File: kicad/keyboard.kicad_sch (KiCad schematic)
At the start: 1 part, among them J1 Conn_02x06_Odd_Even

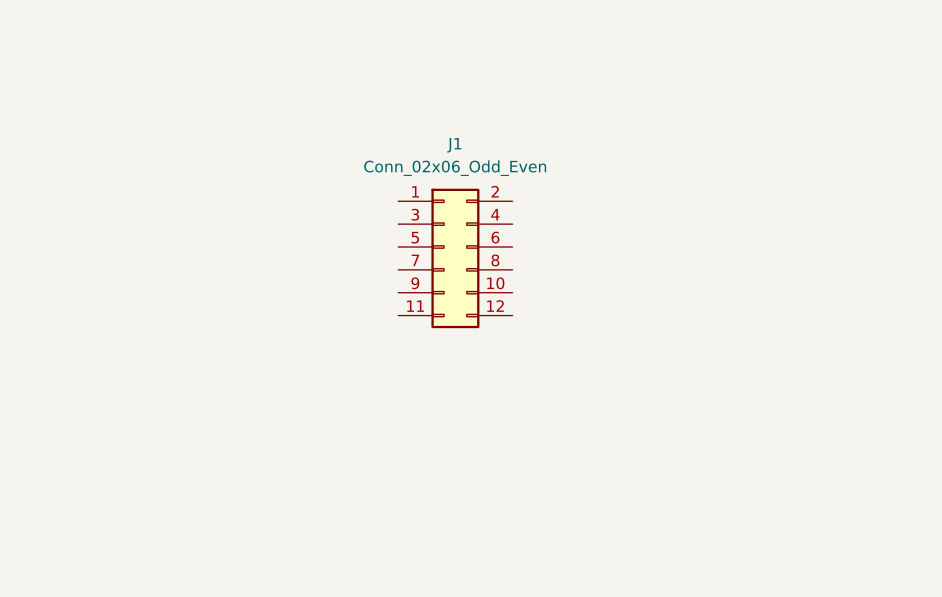
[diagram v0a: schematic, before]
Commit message: Add keyboard connector
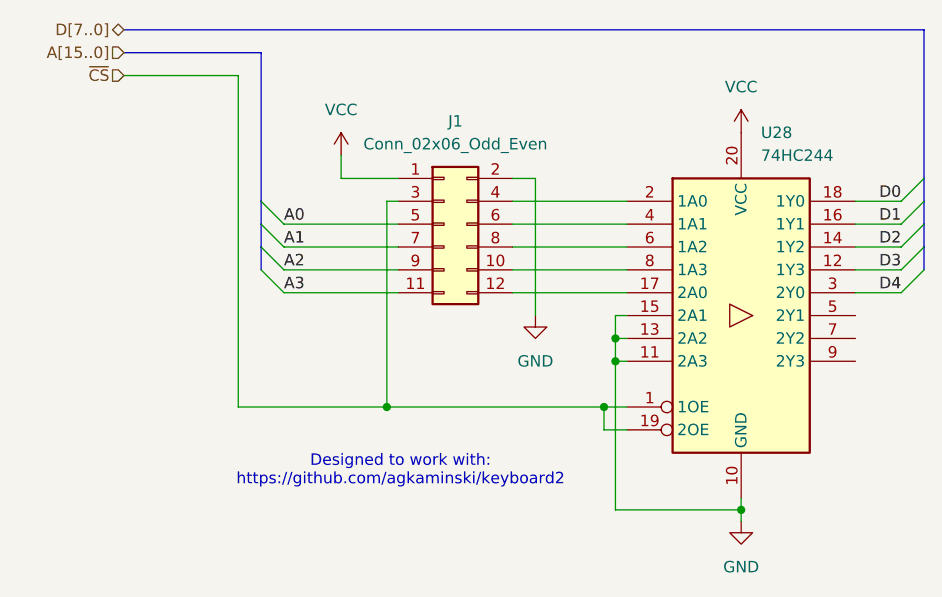
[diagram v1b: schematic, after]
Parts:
- added U28: 74HC244, symbol 74xx:74HC244
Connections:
- net VCC: now reaches J1.1 (Pin_1)
- net VCC: now also U28.20 (VCC)
- net at J1.10 (Pin_10): now also U28.8 (1A3)
- net A3: now reaches J1.11 (Pin_11)
- net at J1.12 (Pin_12): now also U28.17 (2A0)
- net GND: now reaches J1.2 (Pin_2)
- net GND: now also U28.10 (GND), U28.11 (2A3), U28.13 (2A2), U28.15 (2A1)
- net ~{CS}: now reaches J1.3 (Pin_3)
- net ~{CS}: now also U28.1 (1OE), U28.19 (2OE)
- net at J1.4 (Pin_4): now also U28.2 (1A0)
- net A0: now reaches J1.5 (Pin_5)
- net at J1.6 (Pin_6): now also U28.4 (1A1)
- net A1: now reaches J1.7 (Pin_7)
- net at J1.8 (Pin_8): now also U28.6 (1A2)
- net A2: now reaches J1.9 (Pin_9)
- new net D0: U28.18 (1Y0)
- new net D1: U28.16 (1Y1)
- new net D2: U28.14 (1Y2)
- new net D3: U28.12 (1Y3)
- new net D4: U28.3 (2Y0)
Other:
- note added: "Designed to work with: https://github.com/agkaminski/keyboard2"
- moved on the sheet: J1

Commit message: Add user IO and USB
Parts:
- U28: footprint (none) -> Package_DIP:DIP-20_W7.62mm
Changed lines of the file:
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@@
 			)
 		)
-		(property "Footprint" ""
+		(property "Footprint" "Package_DIP:DIP-20_W7.62mm"
 			(at 165.1 129.54 0)
 			(effects

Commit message: Add caps and make initial placement
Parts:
- added C37: 100n, Capacitor_THT:C_Disc_D5.0mm_W2.5mm_P2.50mm, symbol Device:C
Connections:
- net GND: now also C37.2
- net VCC: now also C37.1
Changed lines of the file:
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@@
+	(symbol
+		(lib_id "power:VCC")
+		(at 182.88 143.51 0)
+		(unit 1)
+		(exclude_from_sim no)
+		(in_bom yes)
+		(on_board yes)
+		(dnp no)
+		(fields_autoplaced yes)
+		(property "Reference" "#PWR0157"
+			(at 182.88 147.32 0)
+			(effects
+				(font
+					(size 1.27 1.27)
+				)
+				(hide yes)
+			)
+		)
+		(property "Value" "VCC"
+			(at 182.88 138.43 0)
+			(effects
+				(font
+					(size 1.27 1.27)
+				)
+			)
+		)
+		(property "Footprint" ""
+			(at 182.88 143.51 0)
+			(effects
+				(font
+					(size 1.27 1.27)
+				)
+				(hide yes)
+			)
+		)
+		(property "Datasheet" ""
+			(at 182.88 143.51 0)
+			(effects
+				(font
+					(size 1.27 1.27)
+				)
+				(hide yes)
+			)
+		)
+		(property "Description" "Power symbol creates a global label with name \"VCC\""
+			(at 182.88 143.51 0)
+			(effects
+				(font
+					(size 1.27 1.27)
+				)
+				(hide yes)
+			)
+		)
+		(pin "1"
+		)
+		(instances
+			(project "fella"
+				(path "/0e49b66d-39aa-4a48-b9a1-8037366b6d94/4fcf83d0-a396-4aeb-b2db-c20a053d3b3c"
+					(reference "#PWR0157")
+					(unit 1)
+				)
+			)
+		)
+	)
+	(symbol
+		(lib_id "power:GND")
+		(at 182.88 151.13 0)
+		(unit 1)
+		(exclude_from_sim no)
+		(in_bom yes)
+		(on_board yes)
+		(dnp no)
+		(fields_autoplaced yes)
+		(property "Reference" "#PWR0158"
+			(at 182.88 157.48 0)
+			(effects
+				(font
+					(size 1.27 1.27)
+				)
+				(hide yes)
+			)
+		)
+		(property "Value" "GND"
+			(at 182.88 156.21 0)
+			(effects
+				(font
+					(size 1.27 1.27)
+				)
+			)
+		)
+		(property "Footprint" ""
+			(at 182.88 151.13 0)
+			(effects
+				(font
+					(size 1.27 1.27)
+				)
+				(hide yes)
+			)
+		)
+		(property "Datasheet" ""
+			(at 182.88 151.13 0)
+			(effects
+				(font
+					(size 1.27 1.27)
+				)
+				(hide yes)
+			)
+		)
+		(property "Description" "Power symbol creates a global label with name \"GND\" , ground"
+			(at 182.88 151.13 0)
+			(effects
+				(font
+					(size 1.27 1.27)
+				)
+				(hide yes)
+			)
+		)
+		(pin "1"
+		)
+		(instances
+			(project "fella"
+				(path "/0e49b66d-39aa-4a48-b9a1-8037366b6d94/4fcf83d0-a396-4aeb-b2db-c20a053d3b3c"
+					(reference "#PWR0158")
+					(unit 1)
+				)
+			)
+		)
+	)
 	(symbol
 		(lib_id "power:VCC")
@@
 					(unit 1)
 				)
+			)
+		)
+	)
+	(symbol
+		(lib_id "Device:C")
+		(at 182.88 147.32 0)
+		(unit 1)
+		(exclude_from_sim no)
+		(in_bom yes)
+		(on_board yes)
+		(dnp no)
+		(fields_autoplaced yes)
+		(property "Reference" "C37"
+			(at 186.69 146.0499 0)
+			(effects
+				(font
+					(size 1.27 1.27)
+				)
+				(justify left)
+			)
+		)
+		(property "Value" "100n"
+			(at 186.69 148.5899 0)
+			(effects
+				(font
+					(size 1.27 1.27)
+				)
+				(justify left)
+			)
+		)
+		(property "Footprint" "Capacitor_THT:C_Disc_D5.0mm_W2.5mm_P2.50mm"
+			(at 183.8452 151.13 0)
+			(effects
+				(font
+					(size 1.27 1.27)
+				)
+				(hide yes)
+			)
+		)
+		(property "Datasheet" "~"
+			(at 182.88 147.32 0)
+			(effects
+				(font
+					(size 1.27 1.27)
+				)
+				(hide yes)
+			)
+		)
+		(property "Description" "Unpolarized capacitor"
+			(at 182.88 147.32 0)
+			(effects
+				(font
+					(size 1.27 1.27)
+				)
+				(hide yes)
+			)
+		)
+		(pin "2"
+		)
+		(pin "1"
+		)
+		(instances
+			(project "fella"
+				(path "/0e49b66d-39aa-4a48-b9a1-8037366b6d94/4fcf83d0-a396-4aeb-b2db-c20a053d3b3c"
+					(reference "C37")
+					(unit 1)
+				)

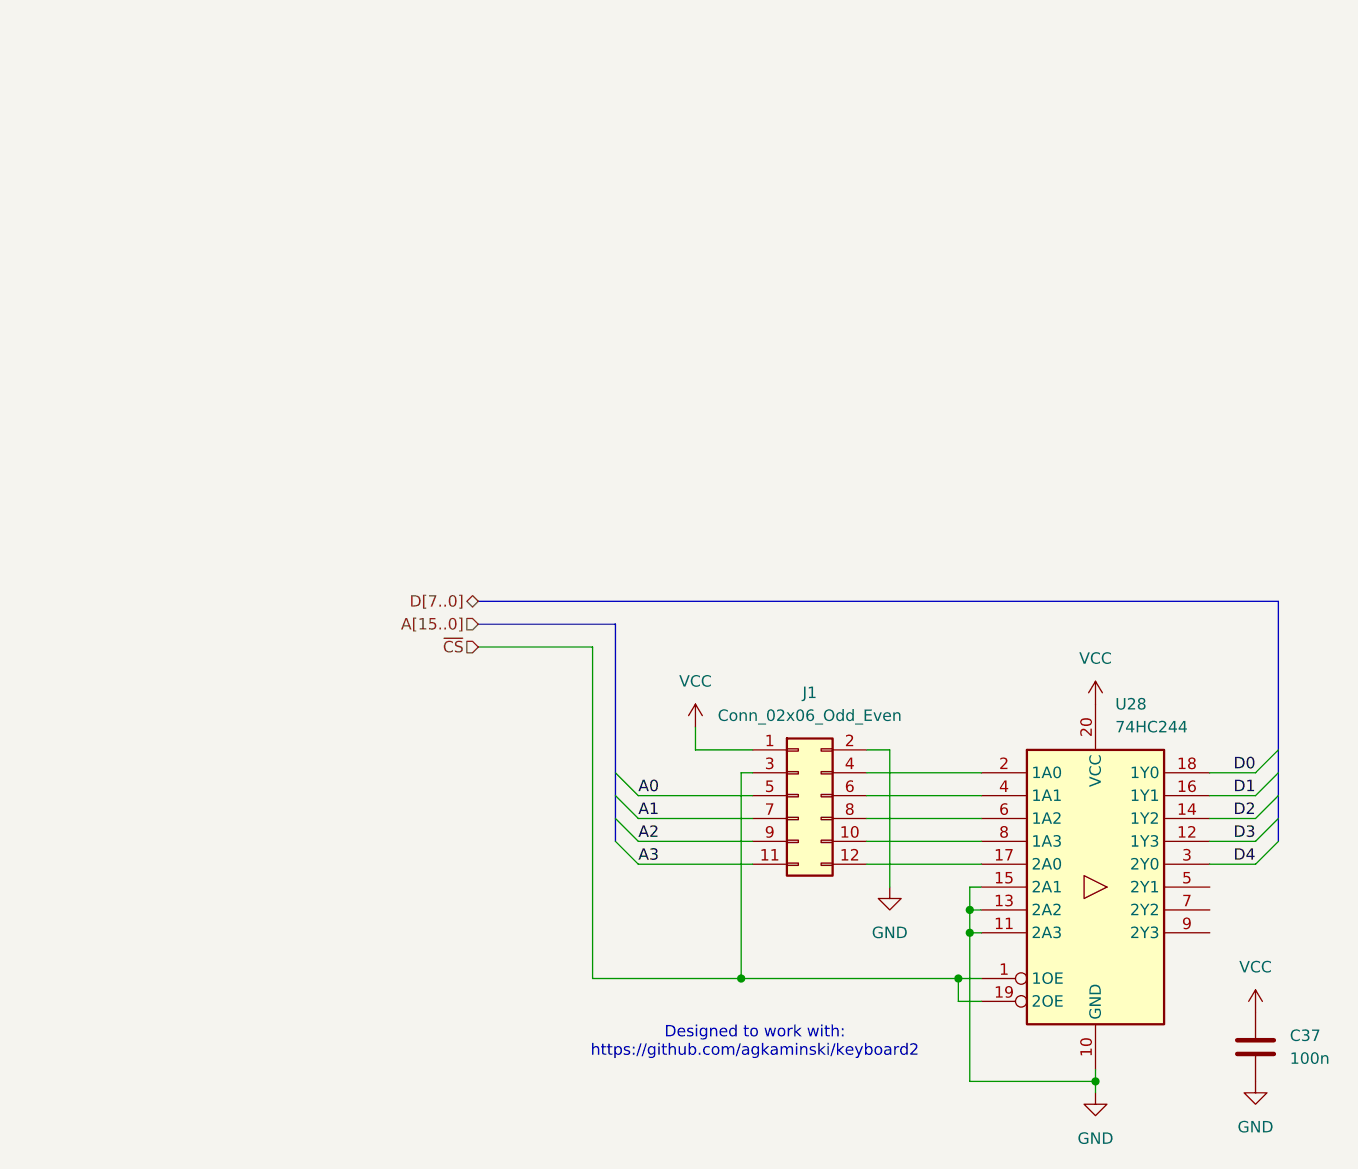
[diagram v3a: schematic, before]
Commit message: hw: revision C
Major changes:
- ROM space has been extended from 16 KiB to 32 KiB
- dynamic RAM option has been removed
- RAM size has been reduced from 32 KiB to 24 KiB
- expansion slot now replaces internal ROM, does not
  have dedicated memory space anymore
- place all I/O within a compactish 8 KiB
- move PH2 gating to /RD and /WR signals
- PCB redo (mechanicaly compatible)
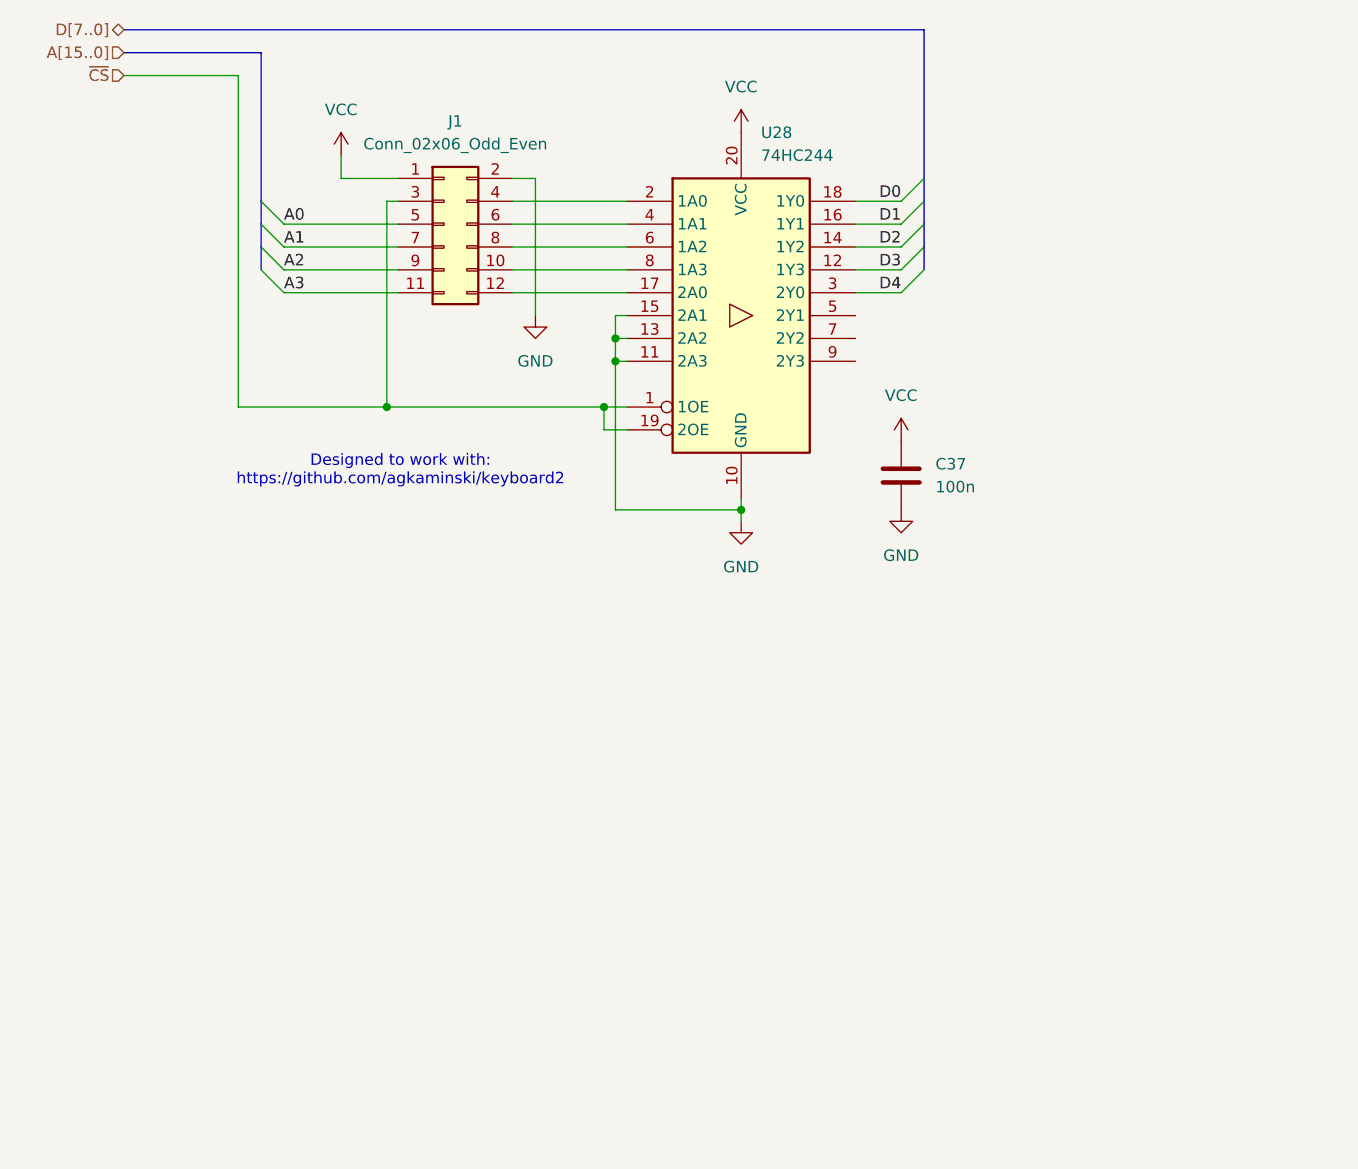
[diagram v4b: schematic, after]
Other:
- moved on the sheet: C37, J1, U28

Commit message: hw: rev D - replace DB25 connector footprint with available one
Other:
- company: (none) -> A.K.
- title: (none) -> Keyboard
